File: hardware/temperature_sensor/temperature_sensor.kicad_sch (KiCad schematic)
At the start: 26 parts, among them J1 Conn_01x02_Male, J2 USB_C_Receptacle_USB2.0_16P, J3 Conn_01x04_Socket, U1 ESP32-C6-MINI-1/U, U2 BME280, U3 MCP1700x-330xxTT, U4 TPD4E02B04DQA

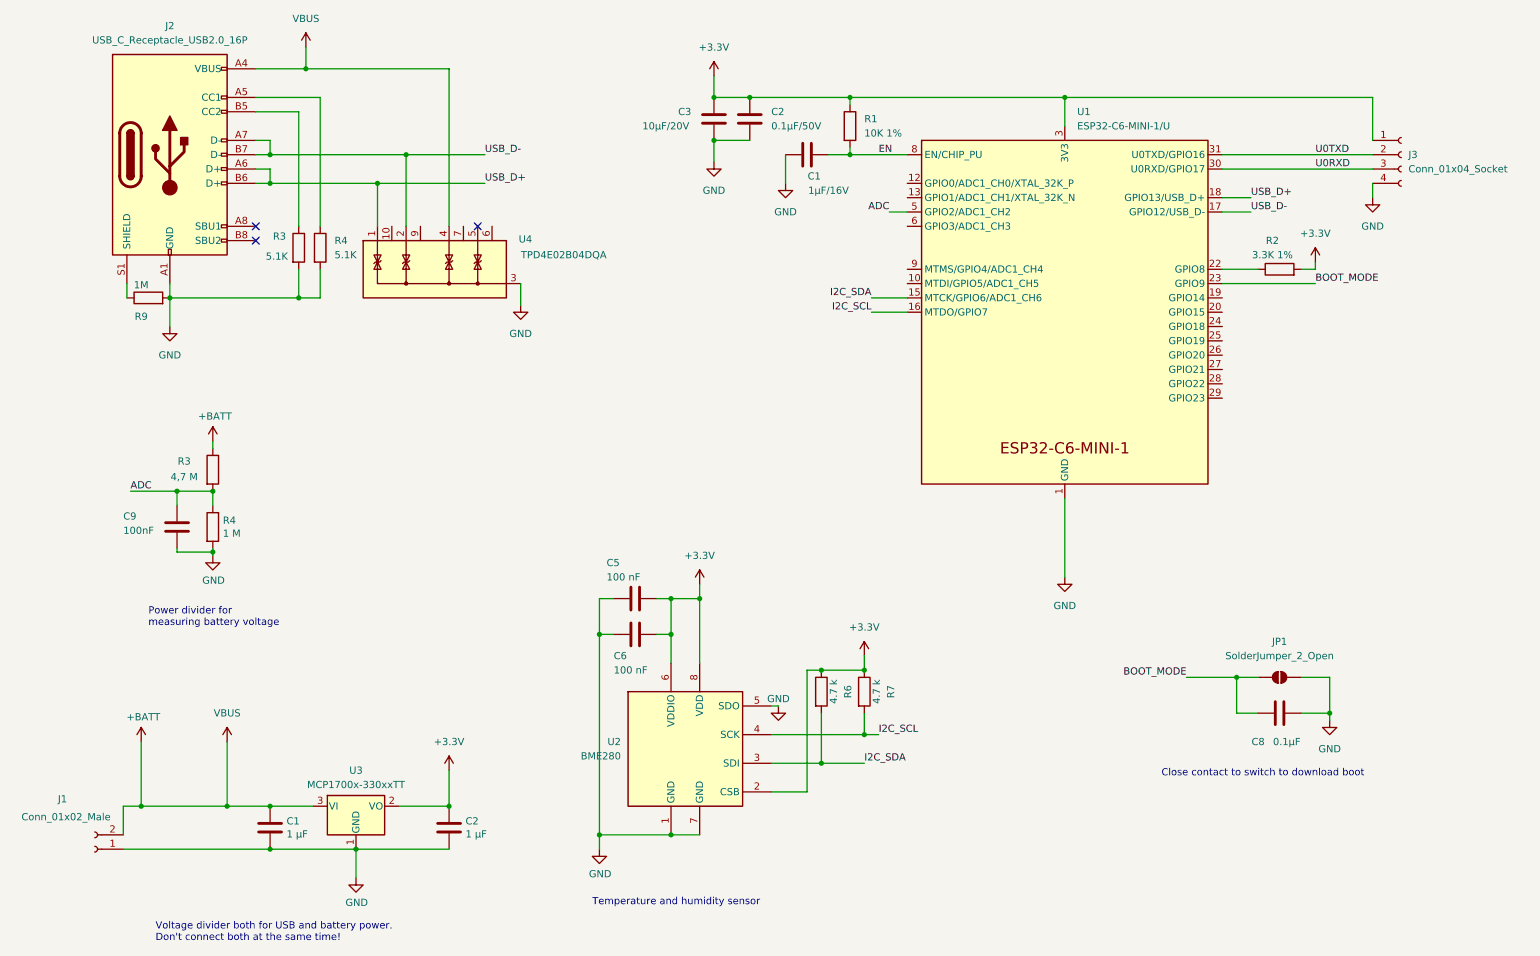
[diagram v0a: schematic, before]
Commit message: Update schema and PCB, more caps, antenna hanging free
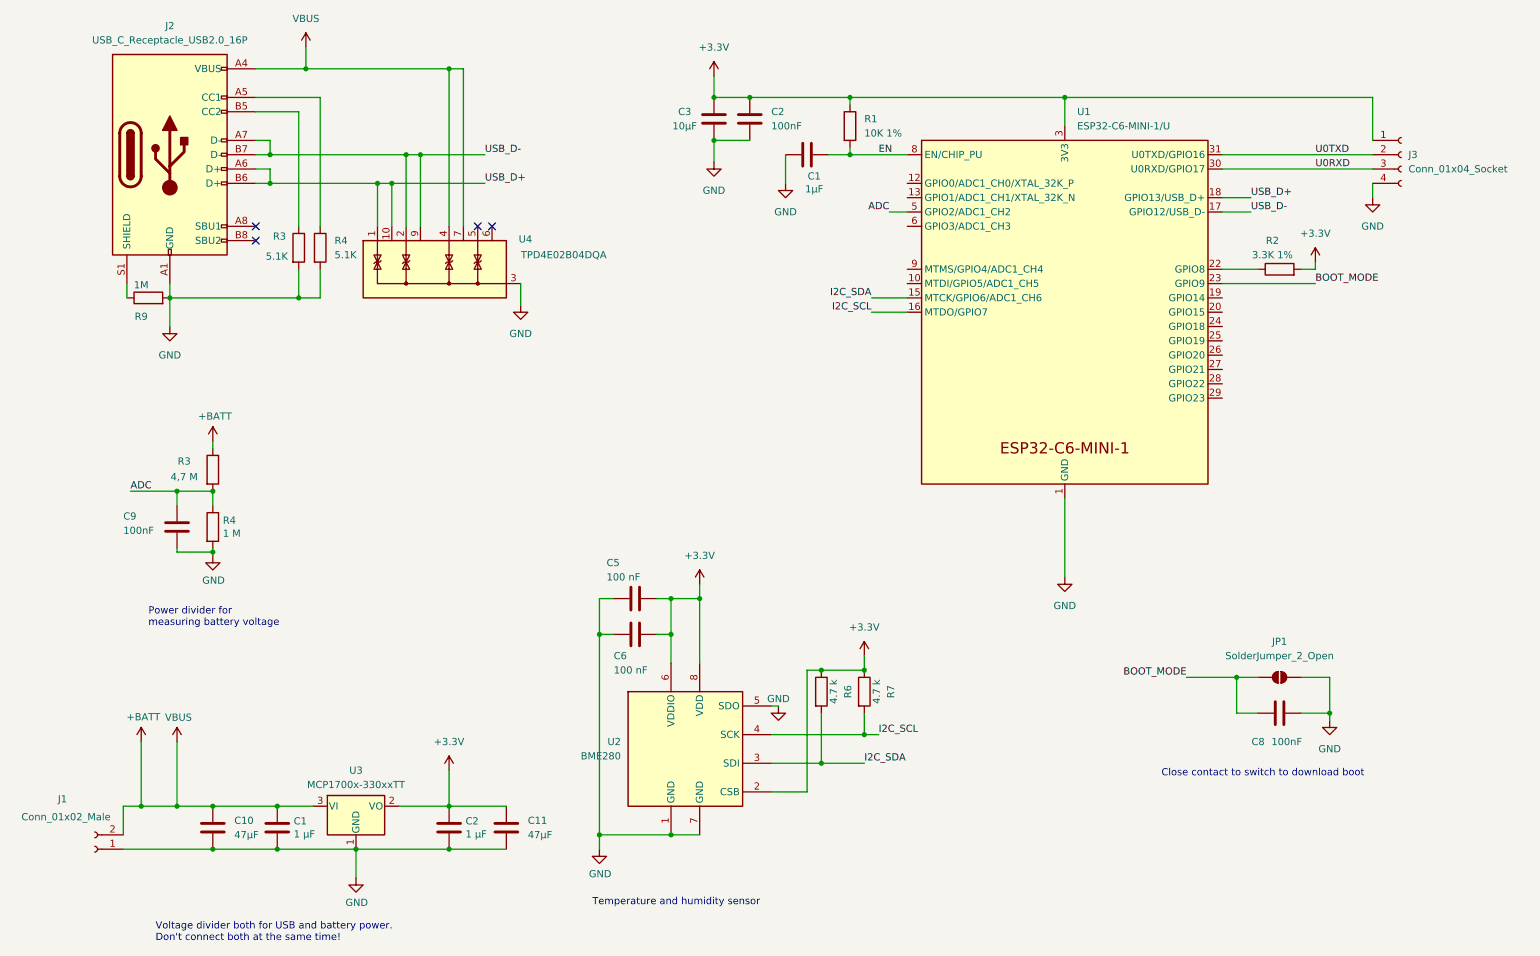
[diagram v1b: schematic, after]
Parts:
- added C10, C11: 47µF, Capacitor_SMD:C_0603_1608Metric, symbol Device:C
- C1: value 1µF/16V -> 1µF
- C2: value 0.1µF/50V -> 100nF
- C3: value 10µF/20V -> 10µF
- C8: value 0.1µF -> 100nF
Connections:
- net +3.3V: now also C11.1
- net +BATT: now also U4.7 (NC), C10.1
- net GND: now also C10.2, C11.2
- net USB_D+: now also U4.10 (NC)
- net USB_D-: now also U4.9 (NC)
- no-connect marks 3 -> 4
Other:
- moved on the sheet: C1
